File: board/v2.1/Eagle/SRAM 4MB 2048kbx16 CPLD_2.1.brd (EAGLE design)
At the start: 50.9 x 49.6 mm, 26 parts, among them IC1 AS6C3216-55, IC2 74LCX245MTC, IC3 74LCX245MTC, IC4 74LCX245MTC, IC5 74LCX541TTR, IC6 74LCX541TTR, IC7 74LCX541TTR, IC8 XC9536XL_44VQ, IC9 TLV70033DDCT, SW1 RAM/Disk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

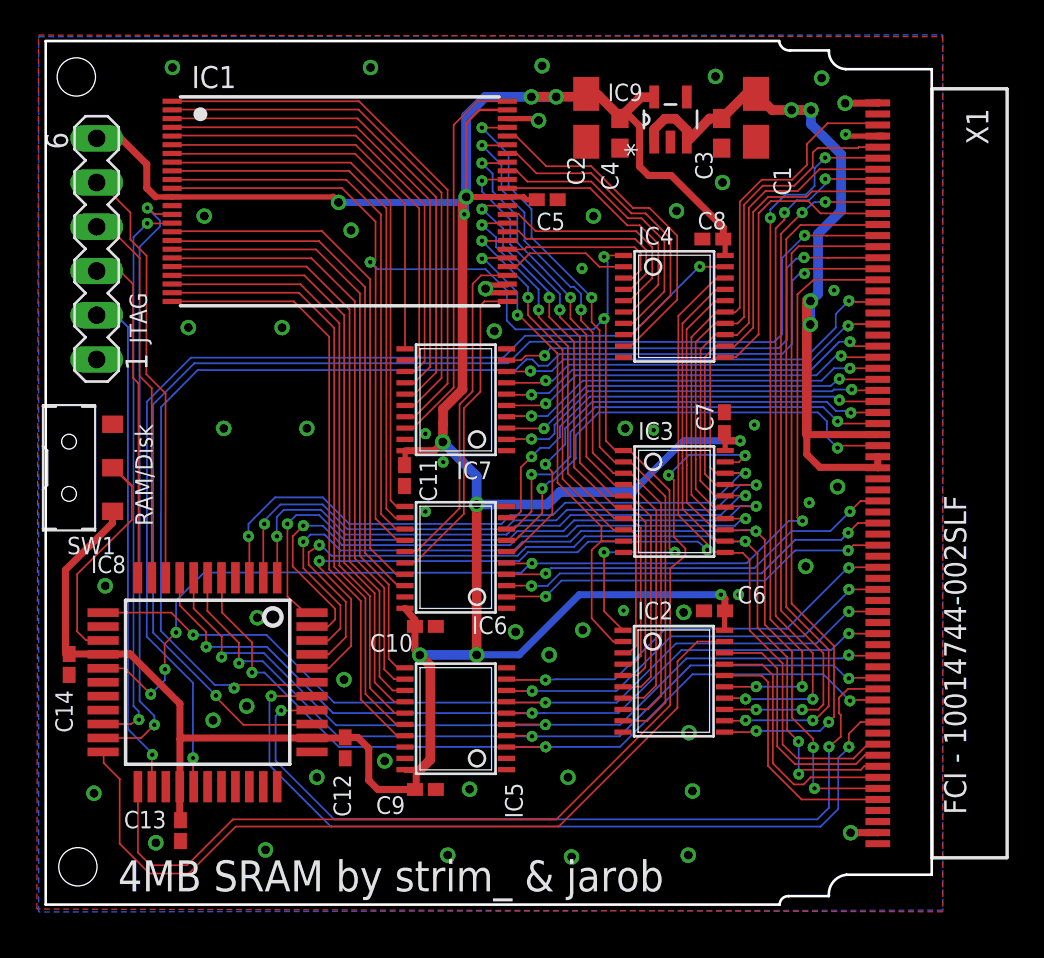
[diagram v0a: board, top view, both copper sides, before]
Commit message: Small change in the boards v2.0 and v2.1
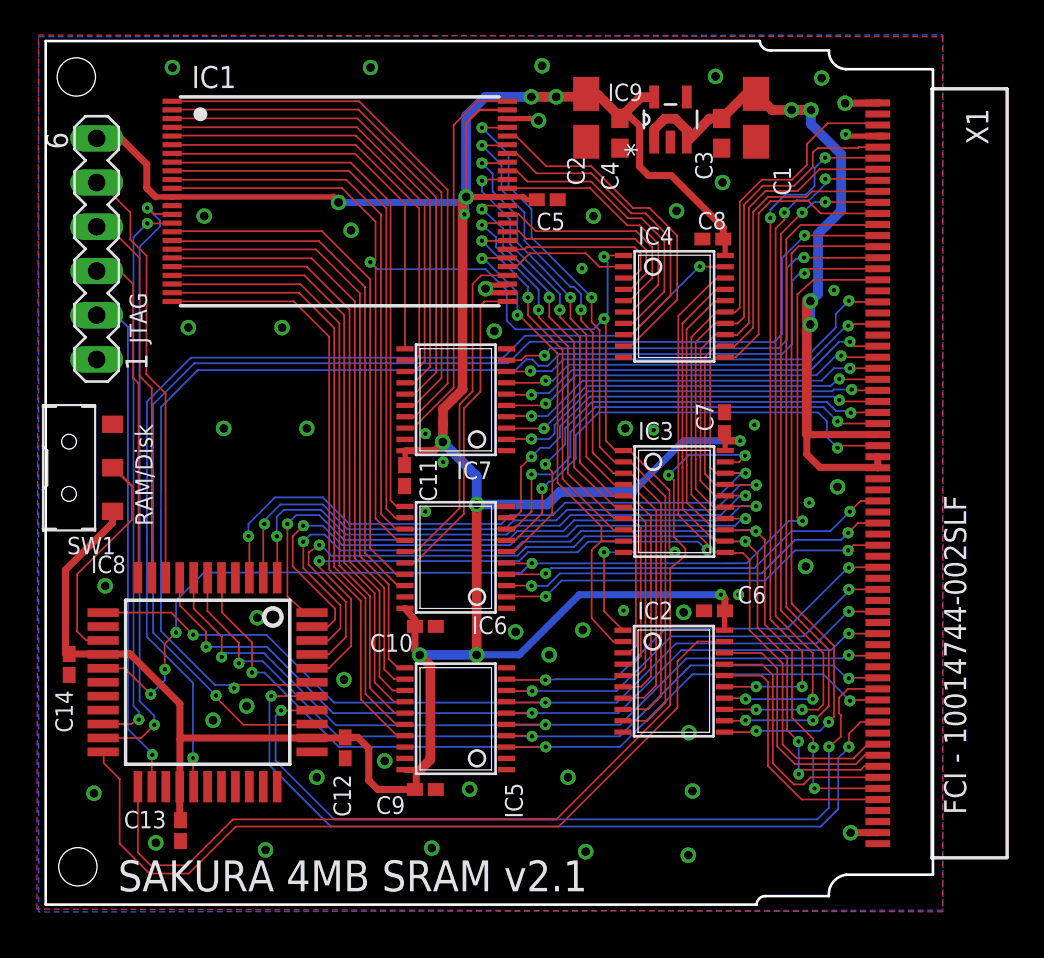
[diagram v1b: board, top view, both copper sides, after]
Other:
- board size 50.9 x 49.6 mm -> 51 x 49.6 mm
- board text added: "SAKURA 4MB SRAM v2.1"
- board text added: "by strim_ & jarob 2014"
- board text removed: "4MB SRAM by strim_ & jarob"
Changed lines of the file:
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@@
 <layer number="24" name="bOrigins" color="15" fill="1" visible="no" active="yes"/>
 <layer number="25" name="tNames" color="7" fill="1" visible="yes" active="yes"/>
-<layer number="26" name="bNames" color="7" fill="1" visible="no" active="yes"/>
+<layer number="26" name="bNames" color="7" fill="1" visible="yes" active="yes"/>
 <layer number="27" name="tValues" color="7" fill="1" visible="yes" active="yes"/>
 <layer number="28" name="bValues" color="7" fill="1" visible="no" active="yes"/>
@@
 <board>
 <plain>
-<wire x1="41.9989" y1="16.94815" x2="84.1502" y2="16.94815" width="0.15" layer="20"/>
-<wire x1="84.1502" y1="16.94815" x2="84.66455" y2="17.4371" width="0.15" layer="20" curve="-90"/>
-<wire x1="84.66455" y1="17.4371" x2="86.9823" y2="17.4371" width="0.15" layer="20"/>
+<wire x1="41.9989" y1="16.94815" x2="82.8294" y2="16.94815" width="0.15" layer="20"/>
+<wire x1="82.8294" y1="16.94815" x2="83.34375" y2="17.4371" width="0.15" layer="20" curve="-90"/>
+<wire x1="83.34375" y1="17.4371" x2="86.9823" y2="17.4371" width="0.15" layer="20"/>
 <wire x1="86.9823" y1="17.4371" x2="87.99195" y2="18.66265" width="0.15" layer="20" curve="-90"/>
-<wire x1="87.99195" y1="18.66265" x2="92.888" y2="18.66265" width="0.15" layer="20"/>
-<wire x1="92.888" y1="18.66265" x2="92.888" y2="64.93145" width="0.15" layer="20"/>
-<wire x1="92.888" y1="64.93145" x2="87.93845" y2="64.93145" width="0.15" layer="20"/>
+<wire x1="87.99195" y1="18.66265" x2="92.95785" y2="18.66265" width="0.15" layer="20"/>
+<wire x1="92.95785" y1="18.66265" x2="92.95785" y2="64.93145" width="0.15" layer="20"/>
+<wire x1="92.95785" y1="64.93145" x2="87.93845" y2="64.93145" width="0.15" layer="20"/>
 <wire x1="87.93845" y1="64.93145" x2="86.9823" y2="66.00825" width="0.15" layer="20" curve="-90"/>
-<wire x1="86.9823" y1="66.00825" x2="84.76615" y2="66.00825" width="0.15" layer="20"/>
-<wire x1="84.76615" y1="66.00825" x2="84.1248" y2="66.548" width="0.15" layer="20" curve="-90"/>
-<wire x1="84.1248" y1="66.548" x2="41.9989" y2="66.548" width="0.15" layer="20"/>
+<wire x1="86.9823" y1="66.00825" x2="83.64855" y2="66.00825" width="0.15" layer="20"/>
+<wire x1="83.64855" y1="66.00825" x2="83.0072" y2="66.548" width="0.15" layer="20" curve="-90"/>
+<wire x1="83.0072" y1="66.548" x2="41.9989" y2="66.548" width="0.15" layer="20"/>
 <wire x1="41.9989" y1="66.548" x2="41.9989" y2="16.94815" width="0.15" layer="20"/>
-<text x="46.1518" y="17.71015" size="1.778" layer="25">4MB SRAM by strim_ &amp; jarob</text>
+<text x="46.1518" y="17.71015" size="1.778" layer="25">SAKURA 4MB SRAM v2.1</text>
 <hole x="43.84675" y="19.11985" drill="2.2"/>
 <hole x="43.75785" y="64.48425" drill="2.2"/>
-<text x="49.3776" y="44.9072" size="1.778" layer="27">SAKURA</text>
-<text x="51.4096" y="41.2496" size="1.778" layer="27">v2.1</text>
+<text x="61.5696" y="45.3136" size="1.778" layer="26" rot="MR0">SAKURA</text>
+<text x="59.8424" y="41.4528" size="1.778" layer="26" rot="MR0">v2.1</text>
+<text x="84.2264" y="20.828" size="1.778" layer="26" rot="MR0">by strim_ &amp; jarob 2014</text>
 </plain>
 <attributes>
@@
 <via x="82.7024" y="44.5008" extent="1-16" drill="0.25"/>
 <via x="81.788" y="34.7472" extent="1-16" drill="0.25"/>
-<via x="72.1995" y="19.685" extent="1-16" drill="0.5"/>
+<via x="73.0123" y="19.9898" extent="1-16" drill="0.5"/>
 <via x="71.9963" y="24.257" extent="1-16" drill="0.5"/>
-<via x="65.0875" y="19.7866" extent="1-16" drill="0.5"/>
+<via x="64.1731" y="20.193" extent="1-16" drill="0.5"/>
 <via x="54.6227" y="20.0914" extent="1-16" drill="0.5"/>
 <via x="57.5691" y="24.257" extent="1-16" drill="0.5"/>
